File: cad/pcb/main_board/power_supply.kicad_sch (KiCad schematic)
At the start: 14 parts, among them U2 TLV75533PDRVR

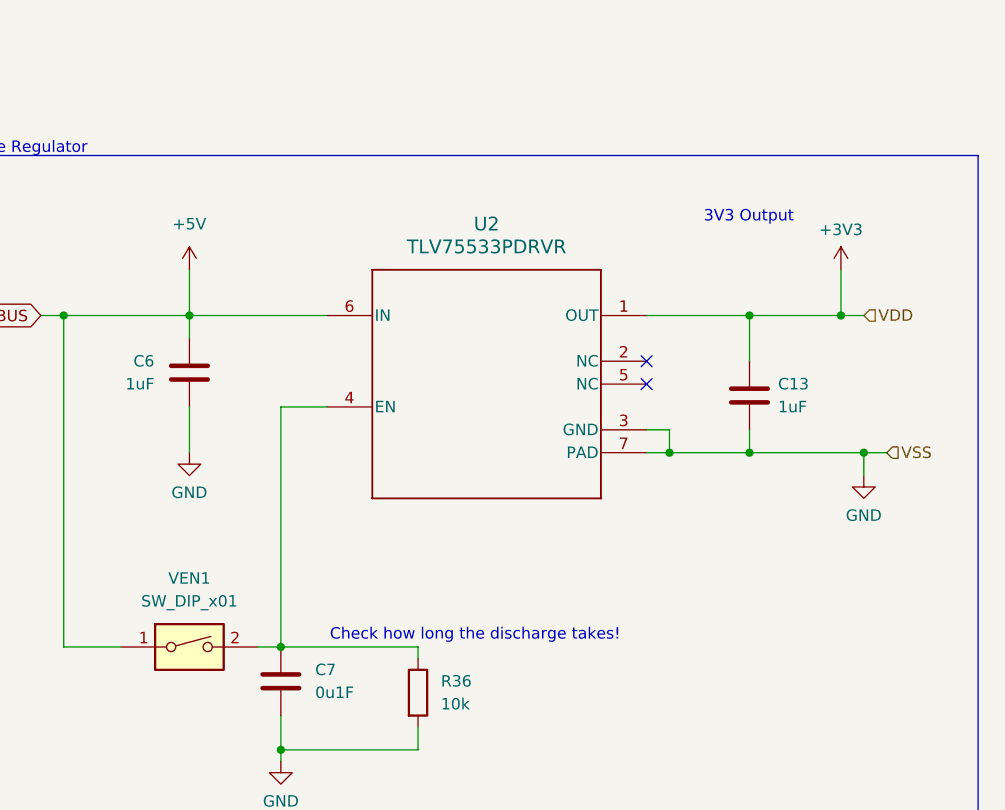
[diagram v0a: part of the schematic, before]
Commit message: Calculating Turn off time, Looking up dropout voltage
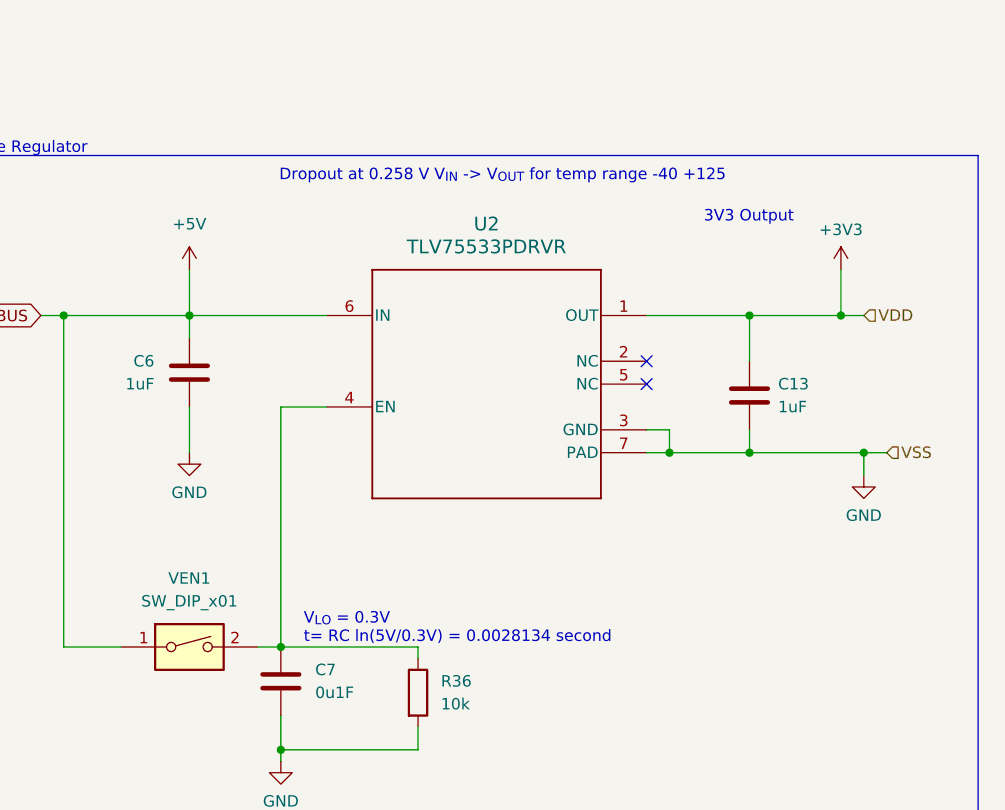
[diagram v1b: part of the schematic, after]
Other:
- note added: "Dropout at 0.258 V V_{IN} -> V_{OUT} for temp range -40 +125"
- note added: "V_{LO} = 0.3V t= RC ln(5V/0.3V) = 0.0028134 second"
- note removed: "Check how long the discharge takes!"
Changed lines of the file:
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@@
+		)
+	)
+	(text "Dropout at 0.258 V V_{IN} -> V_{OUT} for temp range -40 +125"
+		(exclude_from_sim no)
+		(at 114.808 106.426 0)
+		(effects
+			(font
+				(size 1.27 1.27)
+			)
 		)
 	)
@@
 		)
 	)
-	(text "Check how long the discharge takes!"
+	(text "V_{LO} = 0.3V\nt= RC ln(5V/0.3V) = 0.0028134 second"
 		(exclude_from_sim no)
-		(at 111.76 157.48 0)
+		(at 92.71 156.718 0)
 		(effects
 			(font
 				(size 1.27 1.27)
 			)
+			(justify left)
 		)
 	)
